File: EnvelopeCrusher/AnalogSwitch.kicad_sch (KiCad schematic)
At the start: 3 parts, among them U5 DG611E

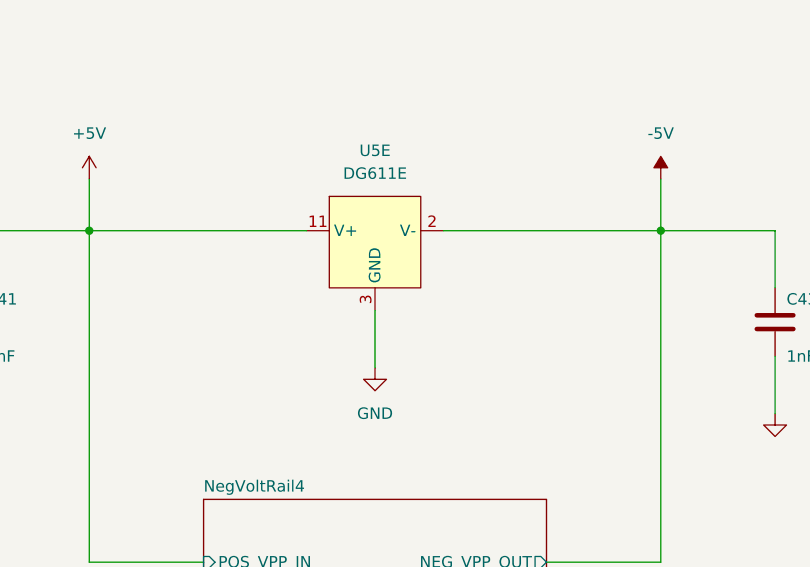
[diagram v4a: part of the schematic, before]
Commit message: Updated footprints/symbol mappings
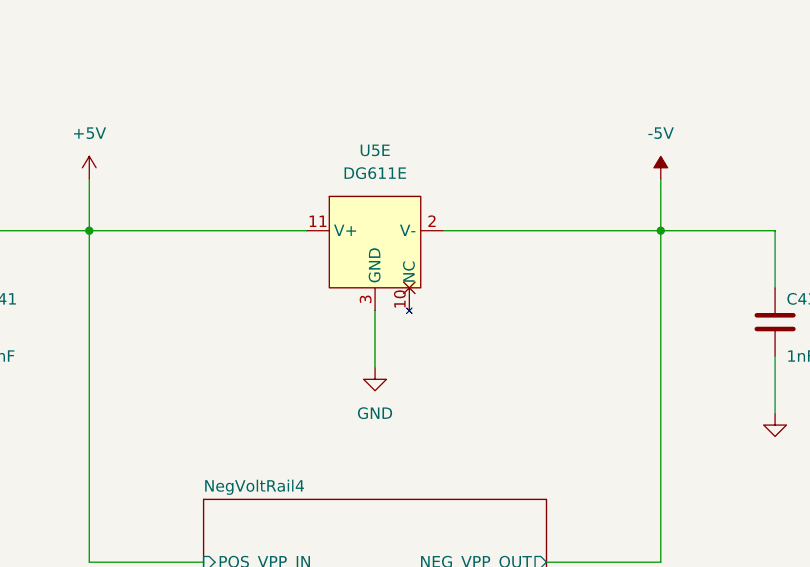
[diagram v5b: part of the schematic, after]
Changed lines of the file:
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@@
     (effects (font (size 1.27 1.27)) (justify right))
   )
-  (symbol (lib_name "DG611E_1") (lib_id "DG61x:DG611E") (at 189.23 214.63 0) (unit 5)
+  (symbol (lib_id "DG61x:DG611E") (at 189.23 214.63 0) (unit 5)
     (in_bom yes) (on_board yes) (fields_autoplaced)
     (property "Reference" "U5" (id 0) (at 189.23 205.74 0))
@@
     (pin "5")
     (pin "6")
+    (pin "10")
     (pin "11")
     (pin "2")
@@
     (pin "1")
   )
-  (symbol (lib_id "DG61x:DG611E") (at 207.01 88.9 0) (unit 2)
+  (symbol (lib_name "DG611E_2") (lib_id "DG61x:DG611E") (at 207.01 88.9 0) (unit 2)
     (in_bom yes) (on_board yes) (fields_autoplaced)
     (property "Reference" "U5" (id 0) (at 207.01 80.01 0))
@@
     (pin "5")
     (pin "6")
+    (pin "10")
     (pin "11")
     (pin "2")
     (pin "3")
   )
-  (symbol (lib_id "DG61x:DG611E") (at 207.01 119.38 0) (unit 3)
+  (symbol (lib_name "DG611E_3") (lib_id "DG61x:DG611E") (at 207.01 119.38 0) (unit 3)
     (in_bom yes) (on_board yes) (fields_autoplaced)
     (property "Reference" "U5" (id 0) (at 207.01 110.49 0))
@@
     (pin "5")
     (pin "6")
+    (pin "10")
     (pin "11")
     (pin "2")
@@
     (pin "2")
   )
-  (symbol (lib_id "DG61x:DG611E") (at 207.01 149.86 0) (unit 4)
+  (symbol (lib_name "DG611E_4") (lib_id "DG61x:DG611E") (at 207.01 149.86 0) (unit 4)
     (in_bom yes) (on_board yes) (fields_autoplaced)
     (property "Reference" "U5" (id 0) (at 207.01 140.97 0))
@@
     (pin "5")
     (pin "6")
+    (pin "10")
     (pin "11")
     (pin "2")
@@
     (pin "1")
   )
-  (symbol (lib_id "DG61x:DG611E") (at 207.01 58.42 0) (unit 1)
+  (symbol (lib_name "DG611E_1") (lib_id "DG61x:DG611E") (at 207.01 58.42 0) (unit 1)
     (in_bom yes) (on_board yes) (fields_autoplaced)
     (property "Reference" "U5" (id 0) (at 207.01 49.53 0))
@@
     (pin "5")
     (pin "6")
+    (pin "10")
     (pin "11")
     (pin "2")

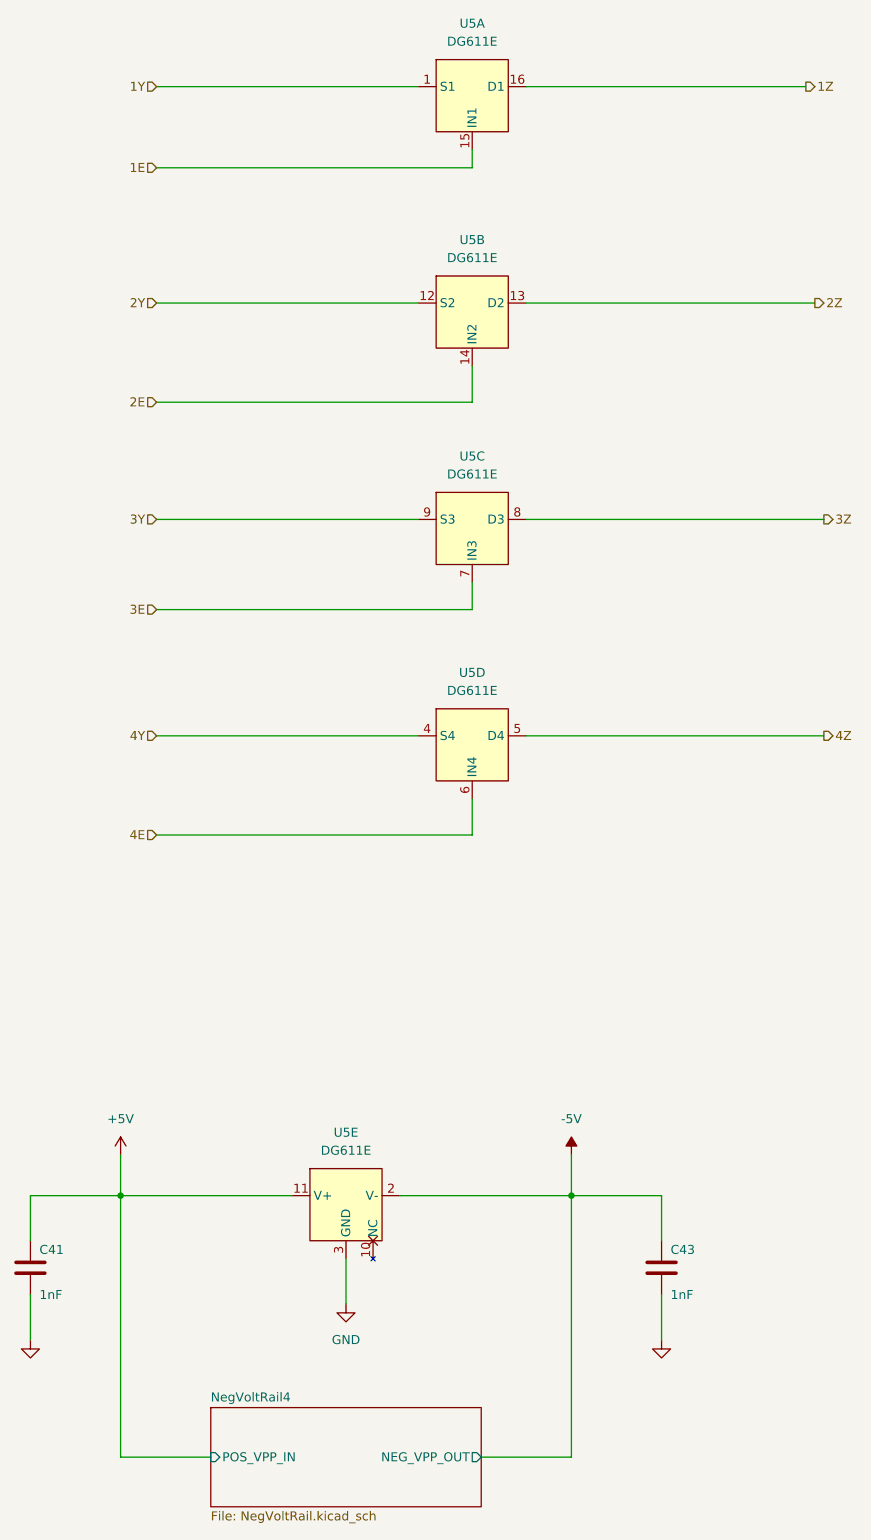
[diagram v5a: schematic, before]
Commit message: organised layout into functional blocks
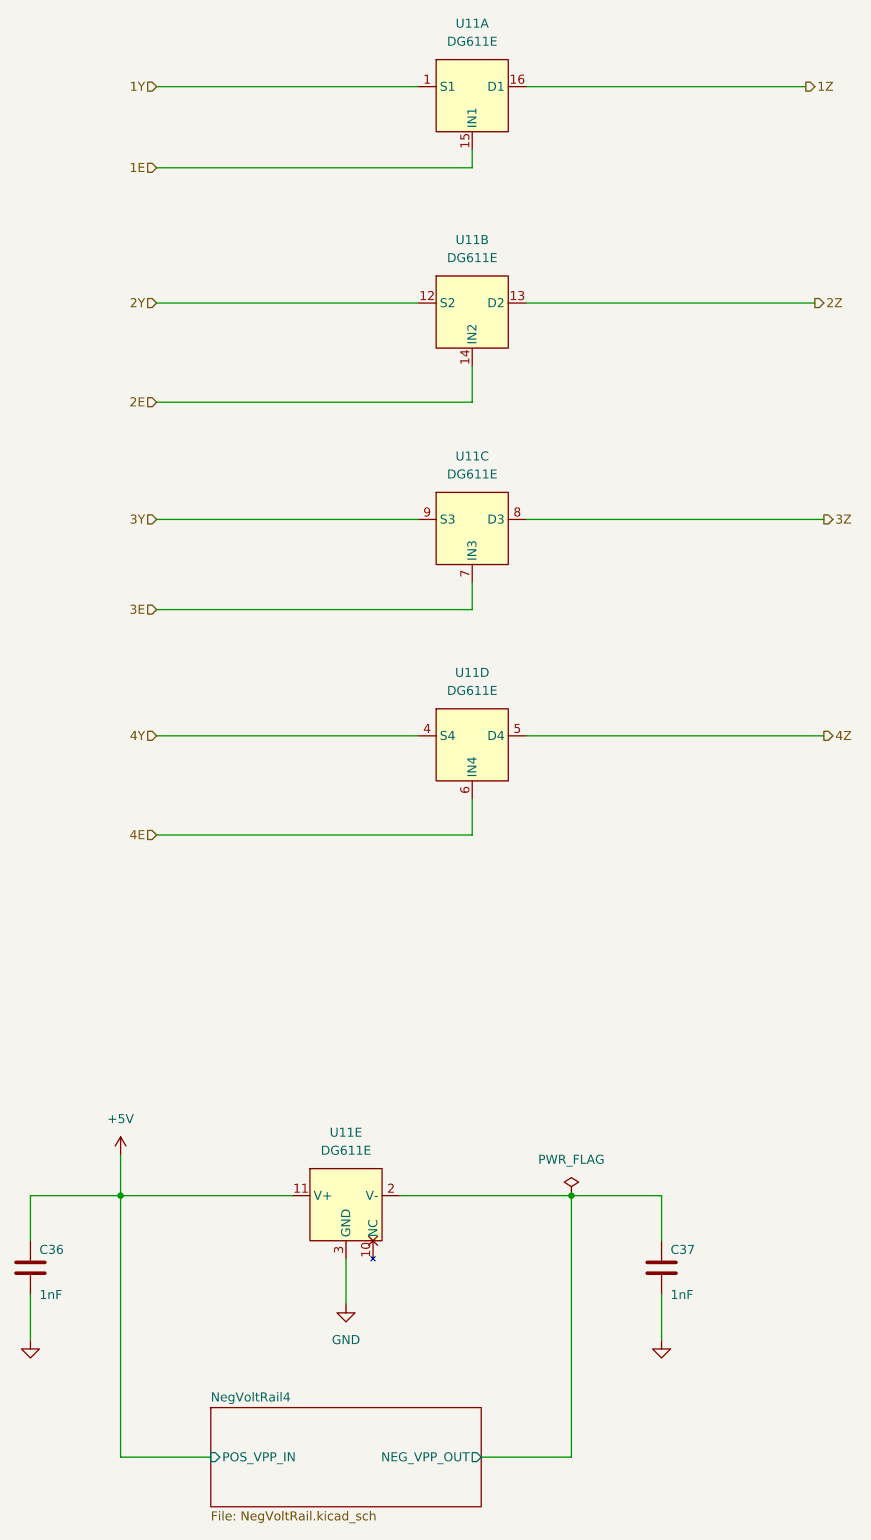
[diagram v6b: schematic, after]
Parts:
- renumbered C41 to C36, C43 to C37, U5 to U11
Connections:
- net -5V renamed NegVoltRail4/NEG_VPP_OUT
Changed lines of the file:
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@@
-    (stroke (width 0) (type default) (color 0 0 0 0))
-  )
-  (wire (pts (xy 220.98 208.9079) (xy 220.98 214.63))
     (stroke (width 0) (type default) (color 0 0 0 0))
   )
@@
   (symbol (lib_id "DG61x:DG611E") (at 189.23 214.63 0) (unit 5)
     (in_bom yes) (on_board yes) (fields_autoplaced)
-    (property "Reference" "U5" (id 0) (at 189.23 205.74 0))
+    (property "Reference" "U11" (id 0) (at 189.23 205.74 0))
     (property "Value" "DG611E" (id 1) (at 189.23 208.28 0))
     (property "Footprint" "ThinMiniQFN:ThinMiniQFN-16_2.6mm_1.8mm" (id 2) (at 189.23 214.63 0)
@@
   (symbol (lib_id "power:+5V") (at 157.48 208.9079 0) (unit 1)
     (in_bom yes) (on_board yes) (fields_autoplaced)
-    (property "Reference" "#PWR061" (id 0) (at 157.48 212.7179 0)
+    (property "Reference" "#PWR059" (id 0) (at 157.48 212.7179 0)
       (effects (font (size 1.27 1.27)) hide)
     )
@@
   (symbol (lib_name "DG611E_2") (lib_id "DG61x:DG611E") (at 207.01 88.9 0) (unit 2)
     (in_bom yes) (on_board yes) (fields_autoplaced)
-    (property "Reference" "U5" (id 0) (at 207.01 80.01 0))
+    (property "Reference" "U11" (id 0) (at 207.01 80.01 0))
     (property "Value" "DG611E" (id 1) (at 207.01 82.55 0))
     (property "Footprint" "ThinMiniQFN:ThinMiniQFN-16_2.6mm_1.8mm" (id 2) (at 207.01 88.9 0)
@@
   (symbol (lib_name "DG611E_3") (lib_id "DG61x:DG611E") (at 207.01 119.38 0) (unit 3)
     (in_bom yes) (on_board yes) (fields_autoplaced)
-    (property "Reference" "U5" (id 0) (at 207.01 110.49 0))
+    (property "Reference" "U11" (id 0) (at 207.01 110.49 0))
     (property "Value" "DG611E" (id 1) (at 207.01 113.03 0))
     (property "Footprint" "ThinMiniQFN:ThinMiniQFN-16_2.6mm_1.8mm" (id 2) (at 207.01 119.38 0)
@@
   (symbol (lib_id "Device:C") (at 144.78 224.79 180) (unit 1)
     (in_bom yes) (on_board yes)
-    (property "Reference" "C41" (id 0) (at 146.05 222.25 0)
+    (property "Reference" "C36" (id 0) (at 146.05 222.25 0)
       (effects (font (size 1.27 1.27)) (justify right))
     )
@@
   (symbol (lib_name "DG611E_4") (lib_id "DG61x:DG611E") (at 207.01 149.86 0) (unit 4)
     (in_bom yes) (on_board yes) (fields_autoplaced)
-    (property "Reference" "U5" (id 0) (at 207.01 140.97 0))
+    (property "Reference" "U11" (id 0) (at 207.01 140.97 0))
     (property "Value" "DG611E" (id 1) (at 207.01 143.51 0))
     (property "Footprint" "ThinMiniQFN:ThinMiniQFN-16_2.6mm_1.8mm" (id 2) (at 207.01 149.86 0)
@@
     (pin "3")
   )
-  (symbol (lib_id "power:-5V") (at 220.98 208.9079 0) (unit 1)
-    (in_bom yes) (on_board yes) (fields_autoplaced)
-    (property "Reference" "#PWR062" (id 0) (at 220.98 206.3679 0)
-      (effects (font (size 1.27 1.27)) hide)
-    )
-    (property "Value" "-5V" (id 1) (at 220.98 203.8279 0))
-    (property "Footprint" "" (id 2) (at 220.98 208.9079 0)
-      (effects (font (size 1.27 1.27)) hide)
-    )
-    (property "Datasheet" "" (id 3) (at 220.98 208.9079 0)
-      (effects (font (size 1.27 1.27)) hide)
-    )
-    (pin "1")
-  )
   (symbol (lib_id "power:GND") (at 233.68 234.95 0) (unit 1)
     (in_bom yes) (on_board yes) (fields_autoplaced)
-    (property "Reference" "#PWR063" (id 0) (at 233.68 241.3 0)
+    (property "Reference" "#PWR061" (id 0) (at 233.68 241.3 0)
       (effects (font (size 1.27 1.27)) hide)
     )
@@
   (symbol (lib_name "DG611E_1") (lib_id "DG61x:DG611E") (at 207.01 58.42 0) (unit 1)
     (in_bom yes) (on_board yes) (fields_autoplaced)
-    (property "Reference" "U5" (id 0) (at 207.01 49.53 0))
+    (property "Reference" "U11" (id 0) (at 207.01 49.53 0))
     (property "Value" "DG611E" (id 1) (at 207.01 52.07 0))
     (property "Footprint" "ThinMiniQFN:ThinMiniQFN-16_2.6mm_1.8mm" (id 2) (at 207.01 58.42 0)
@@
   (symbol (lib_id "power:GND") (at 144.78 234.95 0) (unit 1)
     (in_bom yes) (on_board yes) (fields_autoplaced)
-    (property "Reference" "#PWR060" (id 0) (at 144.78 241.3 0)
+    (property "Reference" "#PWR058" (id 0) (at 144.78 241.3 0)
       (effects (font (size 1.27 1.27)) hide)
     )
@@
   (symbol (lib_id "power:GND") (at 189.23 229.87 0) (unit 1)
     (in_bom yes) (on_board yes) (fields_autoplaced)
-    (property "Reference" "#PWR0100" (id 0) (at 189.23 236.22 0)
+    (property "Reference" "#PWR060" (id 0) (at 189.23 236.22 0)
       (effects (font (size 1.27 1.27)) hide)
     )
@@
   (symbol (lib_id "Device:C") (at 233.68 224.79 180) (unit 1)
     (in_bom yes) (on_board yes)
-    (property "Reference" "C43" (id 0) (at 234.95 222.25 0)
+    (property "Reference" "C37" (id 0) (at 234.95 222.25 0)
       (effects (font (size 1.27 1.27)) (justify right))
     )
@@
     (pin "2")
   )
+  (symbol (lib_id "power:PWR_FLAG") (at 220.98 214.63 0) (unit 1)
+    (in_bom yes) (on_board yes) (fields_autoplaced)
+    (property "Reference" "#FLG06" (id 0) (at 220.98 212.725 0)
+      (effects (font (size 1.27 1.27)) hide)
+    )
+    (property "Value" "PWR_FLAG" (id 1) (at 220.98 209.55 0))
+    (property "Footprint" "" (id 2) (at 220.98 214.63 0)
+      (effects (font (size 1.27 1.27)) hide)
+    )
+    (property "Datasheet" "~" (id 3) (at 220.98 214.63 0)
+      (effects (font (size 1.27 1.27)) hide)
+    )
+    (pin "1")
+  )
   (sheet (at 170.18 244.4821) (size 38.1 13.97) (fields_autoplaced)
